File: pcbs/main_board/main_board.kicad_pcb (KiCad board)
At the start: 2 copper layers, 70 x 61.3 mm, 45 parts, among them J1 BAT1, J2 BAT2, J3 LED strip, J4 Motor, Q1 PMOS, SW1 Power switch, U1 mini_esp32, U2 ADXL345, U3 DRV8873HPWPRQ1, U4 Display, U5 Step-up, U6 TPS22917LDBV, U7 TP4056-42-ESOP8, U8 TC1262-33

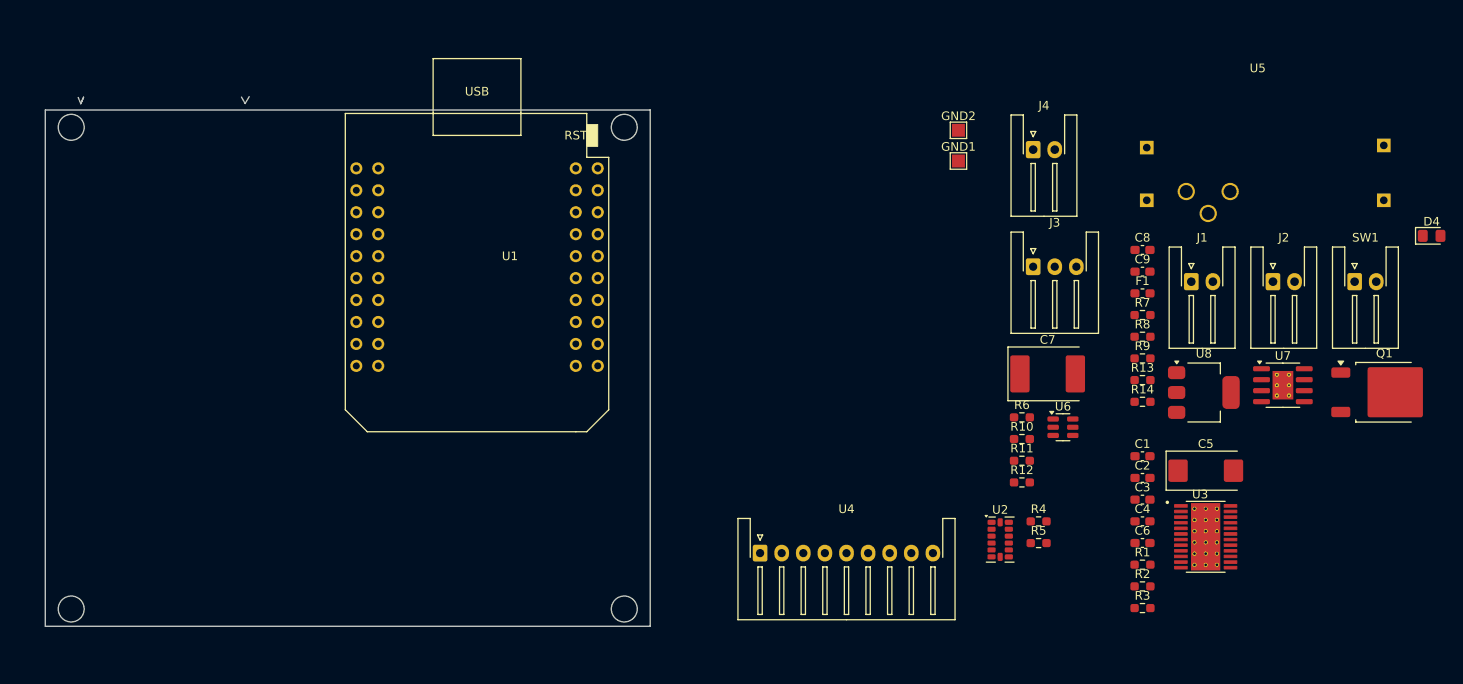
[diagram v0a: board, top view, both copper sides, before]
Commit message: Change 3V3 regulator, add level shifter for led strip
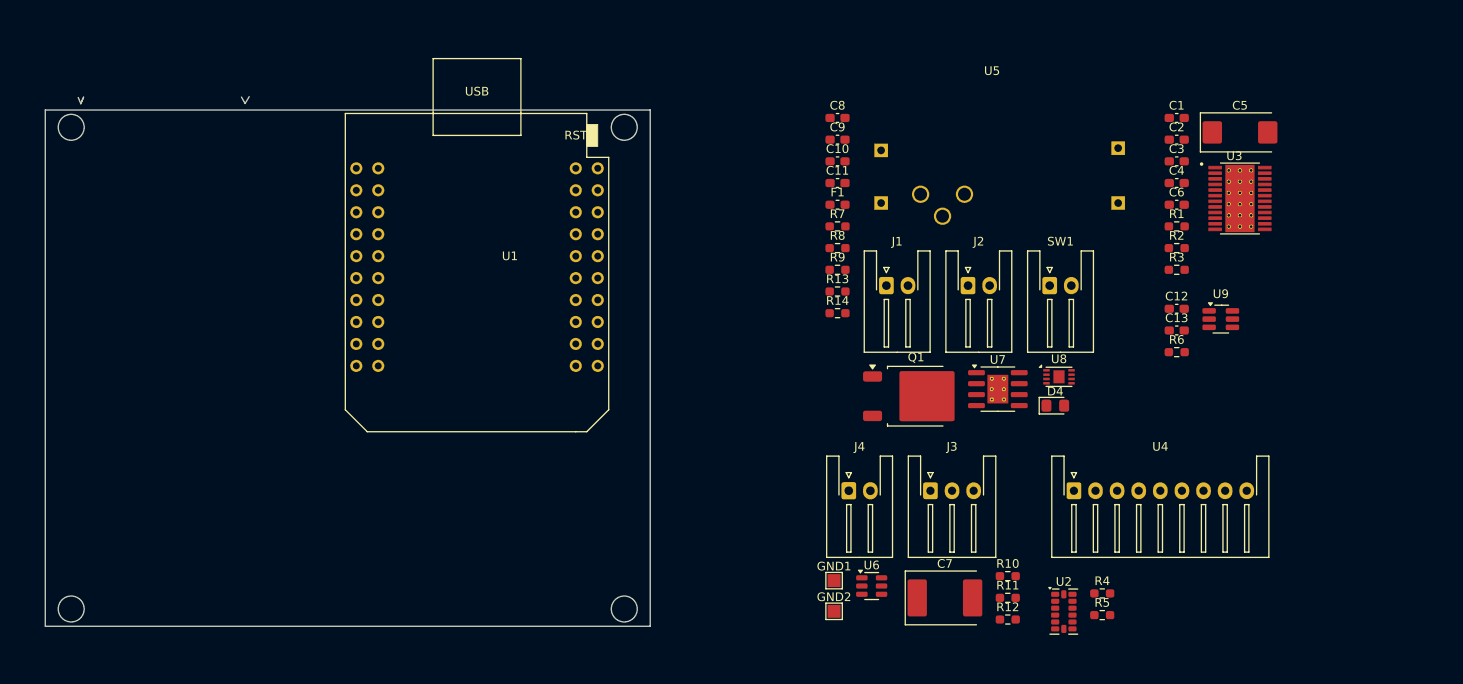
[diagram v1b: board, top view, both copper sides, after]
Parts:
- added C10: 10 uF, Capacitor_SMD:C_0603_1608Metric_Pad1.08x0.95mm_HandSolder, F.Cu at (121.7, 35.9)
- added C11: 10 uF, Capacitor_SMD:C_0603_1608Metric_Pad1.08x0.95mm_HandSolder, F.Cu at (121.7, 38.5)
- added C12: 0.1 uF, Capacitor_SMD:C_0603_1608Metric_Pad1.08x0.95mm_HandSolder, F.Cu at (160.9, 53.0)
- added C13: 0.1 uF, Capacitor_SMD:C_0603_1608Metric_Pad1.08x0.95mm_HandSolder, F.Cu at (160.9, 55.5)
- added U9: TXU0101, Package_TO_SOT_SMD:SOT-23-6_Handsoldering, F.Cu at (166.0, 54.2)
- U8: value TC1262-33 -> ST1L08; footprint Package_TO_SOT_SMD:SOT-223-3_TabPin2 -> Package_DFN_QFN:DFN-8-1EP_3x2mm_P0.5mm_EP1.3x1.5mm
- moved GND2 57.5 mm to (121.3, 88.0)
- moved Q1 54.2 mm to (130.8, 63.1)
- moved GND1 50.6 mm to (121.3, 84.5)
- moved D4 47.8 mm to (146.9, 64.2)
- moved J4 44.9 mm to (123.0, 74.1)
- moved C2 39.3 mm to (160.9, 33.4)
- moved C6 39.3 mm to (160.9, 41.0)
- moved R2 39.3 mm to (160.9, 46.0)
- moved R3 39.3 mm to (160.9, 48.5)
- moved U3 39.3 mm to (168.2, 40.2)
- moved C1 39.3 mm to (160.9, 30.9)
- moved C3 39.3 mm to (160.9, 35.9)
- moved C4 39.3 mm to (160.9, 38.5)
- moved C5 39.3 mm to (168.3, 32.6)
- moved R1 39.3 mm to (160.9, 43.5)
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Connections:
- J3 pad 2: Net-(J3-Pin_2) -> /Level_shifter/OUT
- R6 pad 1: Net-(U1-IO_04) -> /Level_shifter/OUT
- R6 pad 2: Net-(J3-Pin_2) -> Net-(U9-BY)
- U1 pad 32: Net-(U1-IO_04) -> /Level_shifter/IN
- U8 pad 2: GND -> +5V
- U8 pad 3: +3.3V -> unconnected-(U8-NC-Pad3)

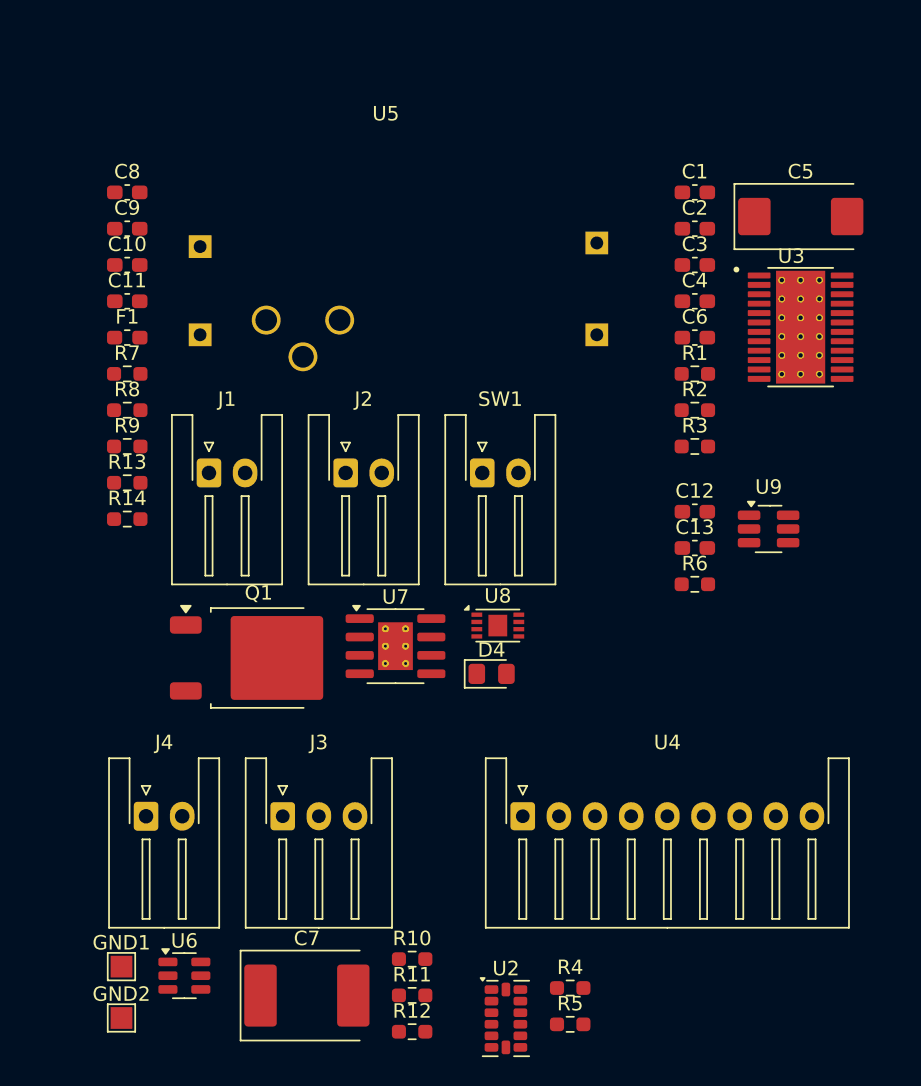
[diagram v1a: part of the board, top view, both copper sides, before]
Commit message: Add LED indicators
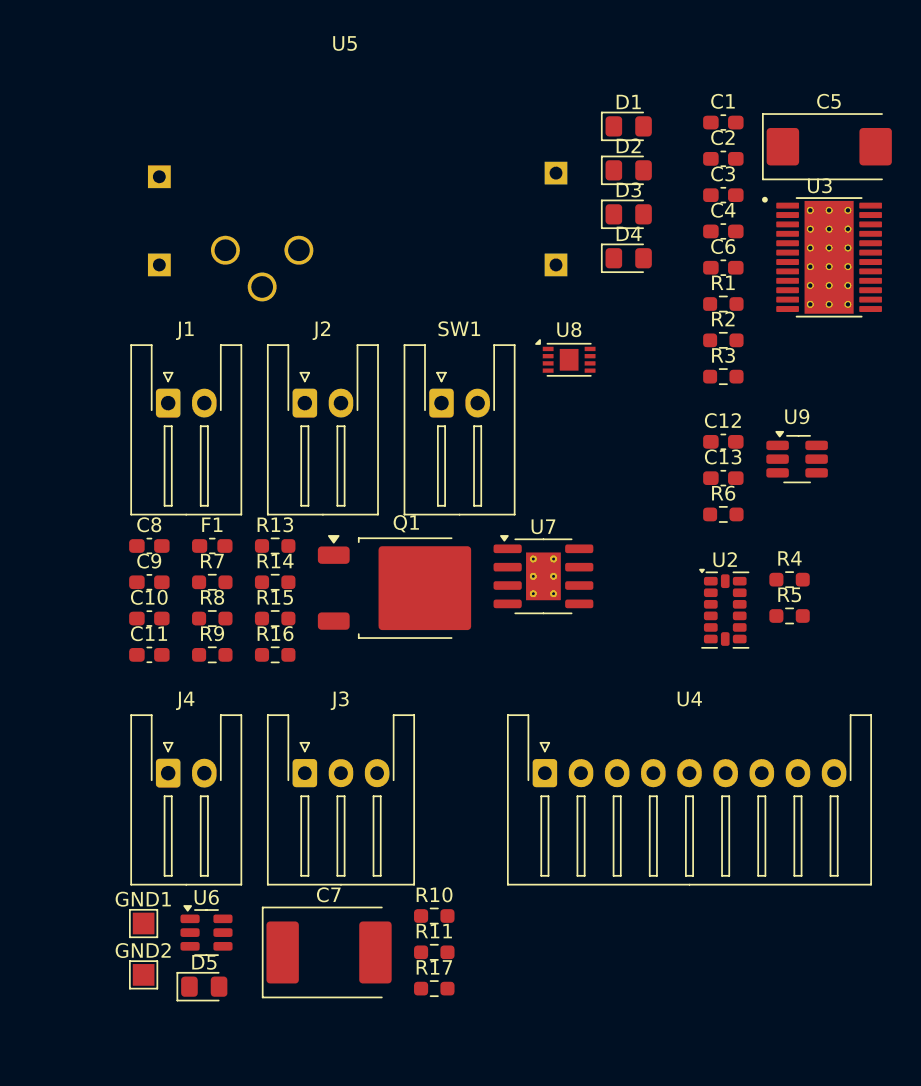
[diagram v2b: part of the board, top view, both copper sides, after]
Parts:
- removed R12: 10k, Resistor_SMD:R_0603_1608Metric_Pad0.98x0.95mm_HandSolder
- added D1: 5V, LED_SMD:LED_0805_2012Metric_Pad1.15x1.40mm_HandSolder, F.Cu at (156.4, 26.4)
- added D2: 3V3, LED_SMD:LED_0805_2012Metric_Pad1.15x1.40mm_HandSolder, F.Cu at (156.4, 29.4)
- added D3: CHARGING, LED_SMD:LED_0805_2012Metric_Pad1.15x1.40mm_HandSolder, F.Cu at (156.4, 32.4)
- added D5: USB, LED_SMD:LED_0805_2012Metric_Pad1.15x1.40mm_HandSolder, F.Cu at (127.0, 85.8)
- added R15: 1k, Resistor_SMD:R_0603_1608Metric_Pad0.98x0.95mm_HandSolder, F.Cu at (131.9, 60.4)
- added R16: 1k, Resistor_SMD:R_0603_1608Metric_Pad0.98x0.95mm_HandSolder, F.Cu at (131.9, 62.9)
- added R17: 2k, Resistor_SMD:R_0603_1608Metric_Pad0.98x0.95mm_HandSolder, F.Cu at (142.9, 86.0)
- D4: value POWER -> BAT
- R13: value 10k -> 2k
- R9: value 1k -> 2k
- moved R5 32.1 mm to (167.5, 60.2)
- moved U2 32.1 mm to (163.0, 59.8)
- moved R4 32.1 mm to (167.5, 57.7)
- moved D4 30.3 mm to (156.4, 35.5)
- moved C10 24.5 mm to (123.2, 60.4)
- moved C9 24.5 mm to (123.2, 57.9)
- moved C11 24.5 mm to (123.2, 62.9)
- moved C8 24.5 mm to (123.2, 55.4)
- moved U8 19.0 mm to (152.2, 42.5)
- moved R7 15.6 mm to (127.6, 57.9)
- moved R8 15.6 mm to (127.6, 60.4)
- moved F1 15.6 mm to (127.6, 55.4)
- moved R9 15.6 mm to (127.6, 62.9)
- moved U7 11.3 mm to (150.5, 57.5)
- moved Q1 11.3 mm to (141.0, 58.3)
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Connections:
- R13 pad 1: /B_CHARGING -> +5V
- R13 pad 2: +3.3V -> Net-(D1-A)

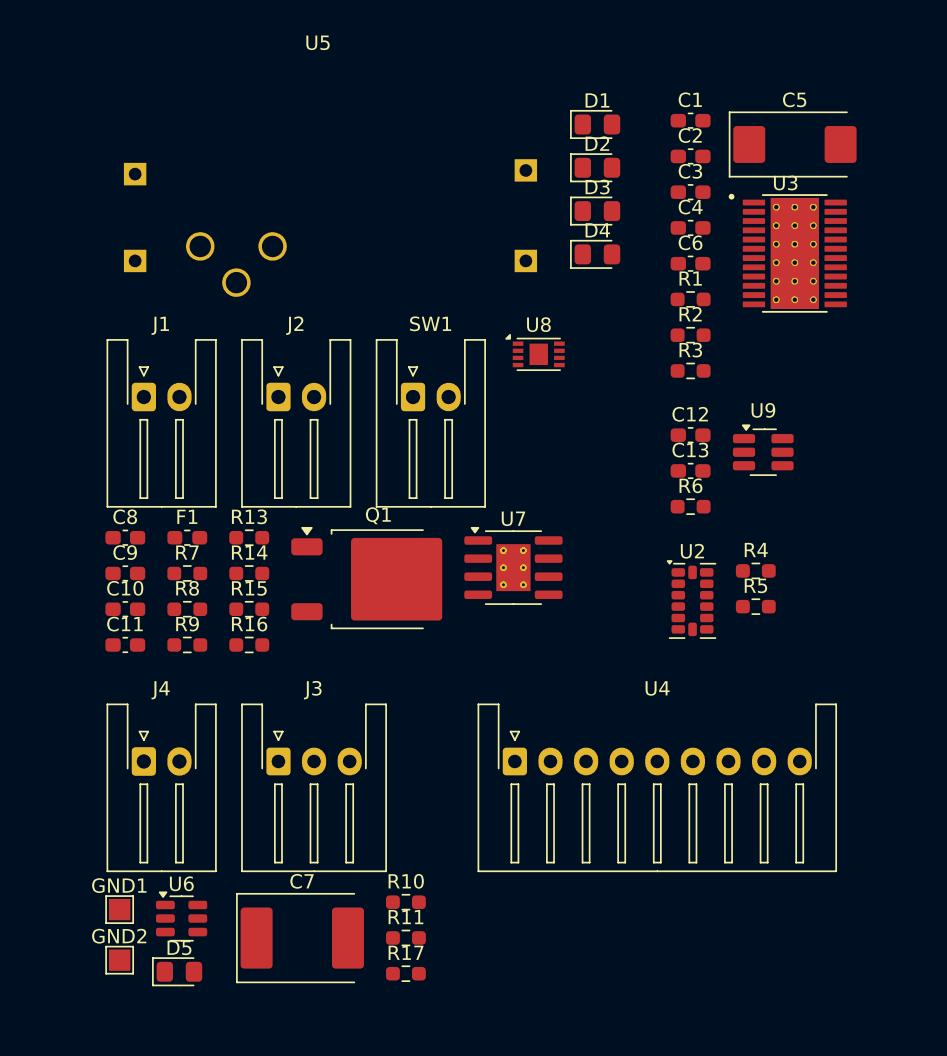
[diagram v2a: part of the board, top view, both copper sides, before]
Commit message: Add reverse polarity protection
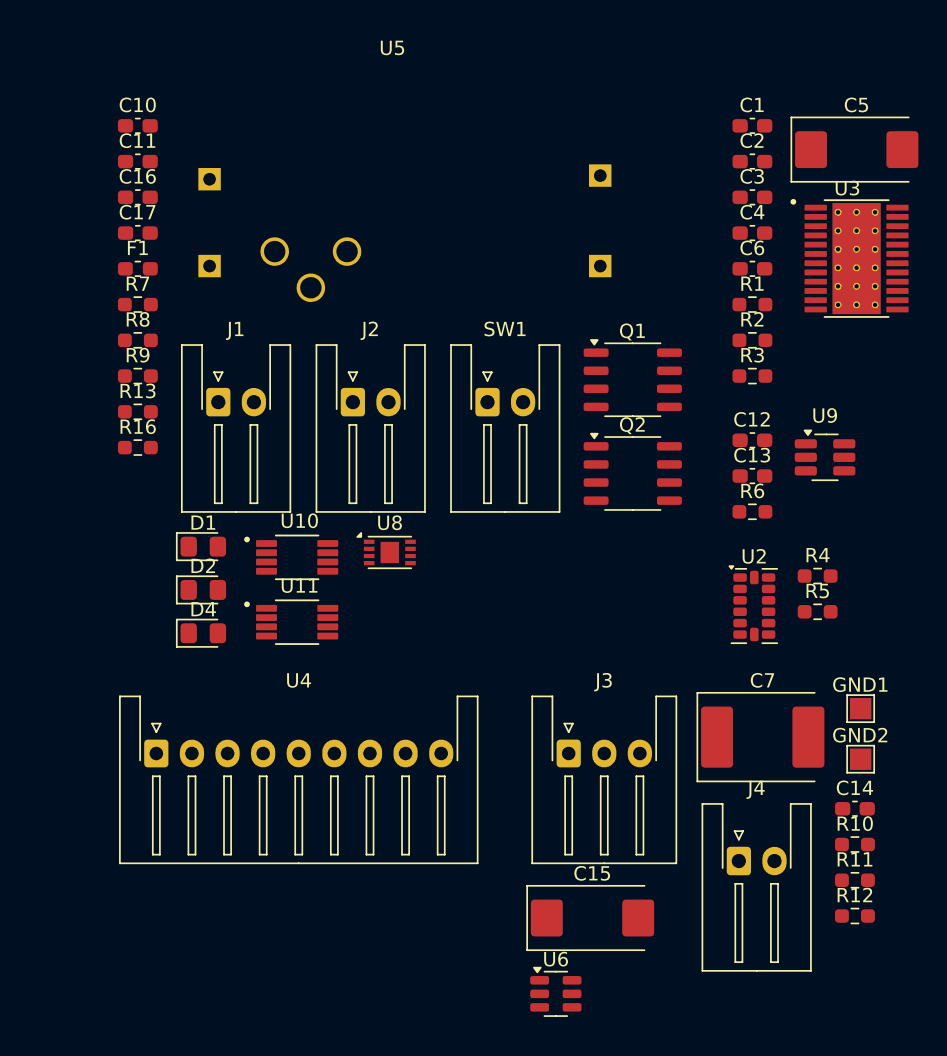
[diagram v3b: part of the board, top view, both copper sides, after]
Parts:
- removed C8, C9: 10 uF, Capacitor_SMD:C_0603_1608Metric_Pad1.08x0.95mm_HandSolder
- removed D3: CHARGING, LED_SMD:LED_0805_2012Metric_Pad1.15x1.40mm_HandSolder
- removed D5: USB, LED_SMD:LED_0805_2012Metric_Pad1.15x1.40mm_HandSolder
- removed R14: 3.01K, Resistor_SMD:R_0603_1608Metric_Pad0.98x0.95mm_HandSolder
- removed R15: 1k, Resistor_SMD:R_0603_1608Metric_Pad0.98x0.95mm_HandSolder
- removed R17: 2k, Resistor_SMD:R_0603_1608Metric_Pad0.98x0.95mm_HandSolder
- removed U7: TP4056-42-ESOP8, Package_SO:SOIC-8-1EP_3.9x4.9mm_P1.27mm_EP2.41x3.3mm_ThermalVias
- added C14: 100 nF, Capacitor_SMD:C_0603_1608Metric_Pad1.08x0.95mm_HandSolder, F.Cu at (174.4, 74.4)
- added C15: 100 uF, Capacitor_Tantalum_SMD:CP_EIA-7343-40_Kemet-Y_HandSolder, F.Cu at (156.0, 82.1)
- added C16: 100 nF, Capacitor_SMD:C_0603_1608Metric_Pad1.08x0.95mm_HandSolder, F.Cu at (124.1, 31.5)
- added C17: 100 nF, Capacitor_SMD:C_0603_1608Metric_Pad1.08x0.95mm_HandSolder, F.Cu at (124.1, 34.0)
- added Q2: NMOS, Package_SO:SO-8_3.9x4.9mm_P1.27mm, F.Cu at (158.8, 50.9)
- added R12: 10k, Resistor_SMD:R_0603_1608Metric_Pad0.98x0.95mm_HandSolder, F.Cu at (174.4, 81.9)
- added U10: LM74610QDGKRQ1, LM74610QDGKRQ1:SOP65P490X110-8N, F.Cu at (135.3, 56.8)
- added U11: LM74610QDGKRQ1, LM74610QDGKRQ1:SOP65P490X110-8N, F.Cu at (135.3, 61.3)
- Q1: value PMOS -> NMOS; footprint Package_TO_SOT_SMD:TO-252-2 -> Package_SO:SO-8_3.9x4.9mm_P1.27mm
- moved GND1 53.9 mm to (174.8, 67.4)
- moved GND2 53.9 mm to (174.8, 70.9)
- moved J4 42.4 mm to (166.3, 78.1)
- moved D1 40.5 mm to (128.7, 56.0)
- moved D2 40.5 mm to (128.7, 59.0)
- moved D4 38.4 mm to (128.7, 62.1)
- moved C7 35.3 mm to (168.0, 69.4)
- moved C10 34.0 mm to (124.1, 26.4)
- moved C11 34.0 mm to (124.1, 29.0)
- moved R10 31.8 mm to (174.4, 76.9)
- moved R11 31.8 mm to (174.4, 79.4)
- moved U6 26.8 mm to (153.4, 87.4)
- moved U4 25.2 mm to (125.4, 70.5)
- moved Q1 22.7 mm to (158.8, 44.3)
- moved J3 20.4 mm to (154.3, 70.5)
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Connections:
- net +5V_USB renamed Net-(U1-VCC_(USB))
- F1 pad 1: Net-(Q1-S) -> Net-(U10-CATHODE)
- J2 pad 2: Net-(J1-Pin_2) -> Net-(J2-Pin_2)
- Q1 pad 2: GND -> Net-(J1-Pin_2)
- Q1 pad 3: Net-(Q1-S) -> Net-(J1-Pin_2)
- U1 pad 7: /B_CHARGING -> unconnected-(U1-IO_35-Pad7)

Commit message: Components update
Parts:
- U4: footprint Connector_JST:JST_XH_S9B-XH-A-1_1x09_P2.50mm_Horizontal -> Connector_JST:JST_XH_S8B-XH-A-1_1x08_P2.50mm_Horizontal
- moved J3 31.4 mm to (123.0, 70.0)
- moved C14 31.4 mm to (143.1, 73.8)
- moved C7 31.4 mm to (136.6, 68.8)
- moved GND1 31.4 mm to (143.5, 66.8)
- moved GND2 31.4 mm to (143.5, 70.4)
- moved J4 31.4 mm to (134.9, 77.5)
- moved R10 31.4 mm to (143.1, 76.4)
- moved R11 31.4 mm to (143.1, 78.9)
- moved R12 31.4 mm to (143.1, 81.4)
- moved U6 31.4 mm to (122.1, 86.8)
- moved C15 31.4 mm to (124.7, 81.5)
- moved U4 25.4 mm to (150.7, 70.0)
- moved C12 2.46 mm to (164.8, 48.0)
- moved C6 2.46 mm to (164.8, 35.9)
- moved D4 2.46 mm to (126.3, 61.5)
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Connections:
- U1 pad 12: /Display/MISO -> unconnected-(U1-IO_23/D7-Pad12)

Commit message: Components update
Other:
- board text added: "NOTES: - Rozměry PCB převzaty z modelu ve Fusionu - navrhl jsem umístění ESP, je potřeba ho umístit někam, kam se snadno vejde USB kabel, takže se klidně může přemístit, ale je třeba na to myslet - Když na to tak koukám, tak se vše pravděpodobně nevejde na jednu stranu, oboustrané PCB nevadí, jen by bylo vhodné dát na stranu FRONT konektory. A podle modelu ve fusionu kouknout kam to na BOTTOM str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"
- board text removed: "NOTES: - Rozměry PCB převzaty z modelu ve Fusionu - navrhl jsem umístění ESP, je potřeba ho umístit někam, kam se snadno vejde USB kabel, takže se klidně může přemýstit, ale je třeba na to myslet - Když na to tak koukám, tak se vše pravděpodobně nevejde na jednu stranu, oboustrané PCB nevadí, jen by bylo vhodné dát na stranu FRONT konektory. A podle modelu ve fusionu kouknout kam to na BOTTOM str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"
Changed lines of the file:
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@@
 		)
 	)
-	(gr_text "NOTES:\n- Rozměry PCB převzaty z modelu ve Fusionu\n- navrhl jsem umístění ESP, je potřeba ho umístit někam, kam se snadno vejde USB kabel, \n  takže se klidně může přemýstit, ale je třeba na to myslet\n- Když na to tak koukám, tak se vše pravděpodobně nevejde na jednu stranu,\n  oboustrané PCB nevadí, jen by bylo vhodné dát na stranu FRONT konektory. A podle modelu\n  ve fusionu kouknout kam to na BOTTOM stranu dát (ne na vertikální středovou osu ani kolem ní).\n- Co se týče konektorů obecně myslet na to, že za hranicí desky už bude stěna. A kabel z té strany\n  nepůjde připojit. Vůbec bych se tedy nebál nechat stranu FRONT pouze konektorům (a ESP), \n  ať se tam konektory strkají lépe.\n- U konektoru na displej je potřeba ohlídat jeho orientaci, případně přečíslovat footprint. \n  Cílem je, aby se kabel od displeje nekřížil, ale šel pěkně rovně. (Konektor displeje se bude\n  nacházet na levé straně (označeno komentářem).\n- Co se šířky cest týče, tak velký proud (4 A) poteče jen BATERIE -- LED PÁSEK\n- Menší výřez z nějaké strany v PCB by mohl být praktický pro protažení kabelů od baterií, \n  LED pásku a motoru."
+	(gr_text "NOTES:\n- Rozměry PCB převzaty z modelu ve Fusionu\n- navrhl jsem umístění ESP, je potřeba ho umístit někam, kam se snadno vejde USB kabel, \n  takže se klidně může přemístit, ale je třeba na to myslet\n- Když na to tak koukám, tak se vše pravděpodobně nevejde na jednu stranu,\n  oboustrané PCB nevadí, jen by bylo vhodné dát na stranu FRONT konektory. A podle modelu\n  ve fusionu kouknout kam to na BOTTOM stranu dát.\n- Co se týče konektorů obecně myslet na to, že za hranicí desky už bude stěna. A kabel z té strany\n  nepůjde připojit. Vůbec bych se tedy nebál nechat stranu FRONT pouze konektorům (a ESP), \n  ať se tam konektory strkají lépe.\n- U konektoru na displej je potřeba ohlídat jeho orientaci, případně přečíslovat footprint. \n  Cílem je, aby se kabel od displeje nekřížil, ale šel pěkně rovně. (Konektor displeje se bude\n  nacházet na levé straně (označeno komentářem).\n- Co se šířky cest týče, tak velký proud (4 A) poteče jen BATERIE -- LED PÁSEK\n- Menší výřez z nějaké strany v PCB by mohl být praktický pro protažení kabelů od baterií, \n  LED pásku a motoru."
 		(at 18.44 108.41 0)
 		(layer "Dwgs.User")
